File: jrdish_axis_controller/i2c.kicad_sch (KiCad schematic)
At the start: 15 parts, among them CN7 SM04B-SRSS-TB (LF)(SN), CN8 SM04B-SRSS-TB (LF)(SN), U5 LTC4311ISC6#TRPBF, U6 LM75BIMX-5/NOPB, U7 W25Q32JVSSIQ_C179173

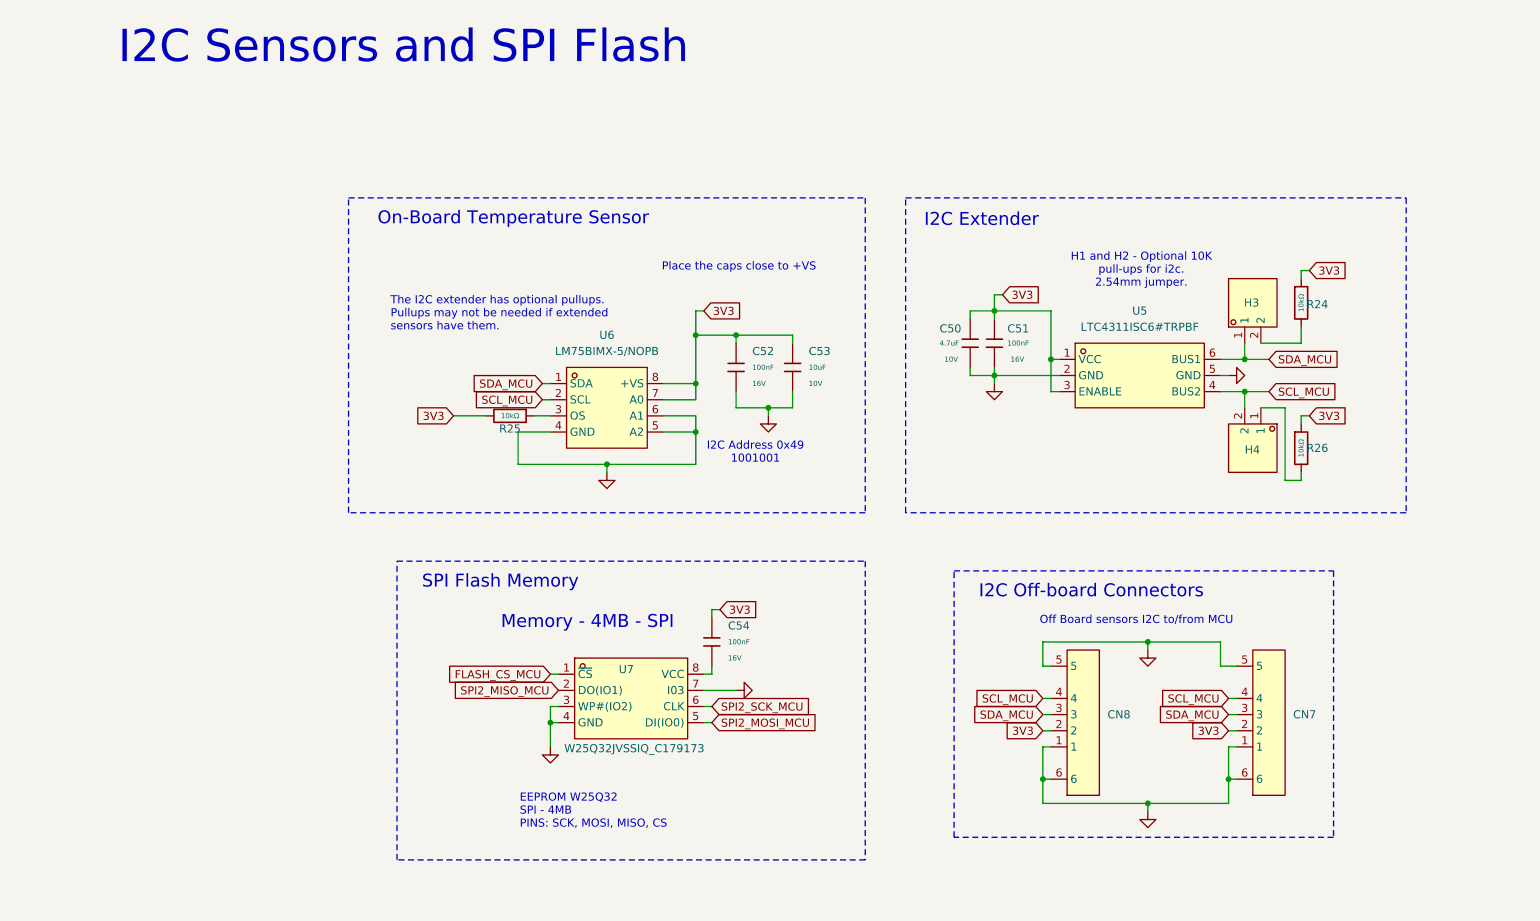
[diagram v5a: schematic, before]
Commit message: RS485 isolated areas in place
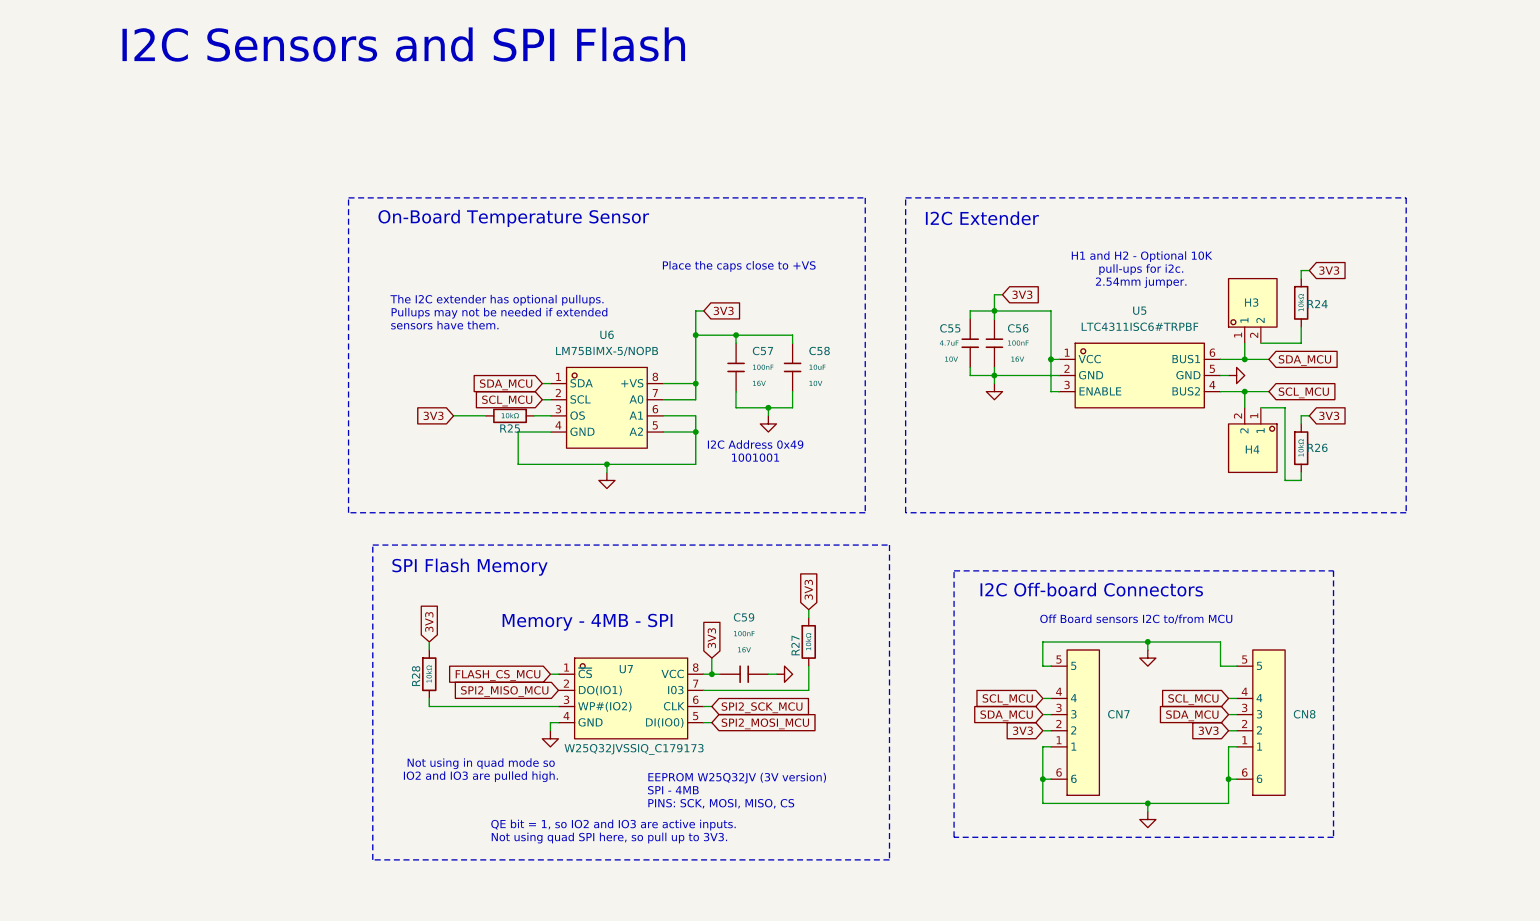
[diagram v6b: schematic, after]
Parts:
- added R27, R28: 10kΩ, PCM_JLCPCB:R_0402, symbol PCM_JLCPCB-Resistors:0402,10kΩ
- renumbered C50 to C55, C51 to C56, C52 to C57, C53 to C58, C54 to C59, CN8 to CN7, CN7 to CN8
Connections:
- net 3V3: now also U7.8 (VCC), R27.1, R28.1
- net GND: now also C59.2; no longer U7.3 (WP#(IO2)), U7.7 (I03)
- new net: R27.2, U7.7 (I03)
- new net: R28.2, U7.3 (WP#(IO2))
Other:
- note added: "EEPROM W25Q32JV (3V version) SPI - 4MB PINS: SCK, MOSI, MISO, CS"
- note added: "Not using in quad mode so IO2 and IO3 are pulled high."
- note added: "QE bit = 1, so IO2 and IO3 are active inputs. Not using quad SPI here, so pull up to 3V3."
- note removed: "EEPROM W25Q32 SPI - 4MB PINS: SCK, MOSI, MISO, CS"
- moved on the sheet: C59

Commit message: Making refinements
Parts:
- added R64: 10kΩ, PCM_JLCPCB:R_0402, symbol PCM_JLCPCB-Resistors:0402,10kΩ
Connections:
- net 3V3: now also R64.1
- net FLASH_CS_MCU: now also R64.2
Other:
- note added: "H3/H4 are the I2C pull-up resistors. Jumper should be in place by default, unless an external module supplies pull-up resistors."
- note added: "SPI Flash Memory - 4MB"
- note removed: "Memory - 4MB - SPI"
- note removed: "SPI Flash Memory"
- moved on the sheet: R28

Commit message: Making refinements
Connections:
- removed net GND: C55.2, C56.2, C57.2, C58.2, C59.2, CN7.1, CN7.5, CN7.6, CN8.1, CN8.5, CN8.6, U5.2 (GND), U5.5 (GND), U6.4 (GND), U6.5 (A2), U6.6 (A1), U7.4 (GND)
- new net: U6.4 (GND), U6.5 (A2), U6.6 (A1)
- new net: C55.2, C56.2, U5.2 (GND)
- new net: C57.2, C58.2
- new net: CN7.1, CN7.6, CN8.1, CN8.6
- new net: CN7.5, CN8.5
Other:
- note added: "NOR Flash W25Q32JV (3V version) SPI - 4MB PINS: SCK, MOSI, MISO, CS"
- note removed: "EEPROM W25Q32JV (3V version) SPI - 4MB PINS: SCK, MOSI, MISO, CS"
- title: (none) -> I2C and I2C Flash
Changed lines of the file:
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@@
 	(paper "A4")
 	(title_block
-		(date "2026-04-12")
+		(title "I2C and I2C Flash")
+		(date "2026-04-30")
 		(rev "1.0")
 		(company "JRSeti")
 	)
 	(rectangle
-		(start 66.04 100.33)
+		(start 59.69 100.33)
 		(end 147.32 149.86)
 		(stroke
@@
 		)
 	)
-	(text "EEPROM W25Q32JV (3V version) \nSPI - 4MB \nPINS: SCK, MOSI, MISO, CS"
+	(text "NOR Flash W25Q32JV (3V version) \nSPI - 4MB \nPINS: SCK, MOSI, MISO, CS"
 		(exclude_from_sim no)
 		(at 109.22 139.192 0)
@@
 			)
 		)
-		(property "Datasheet" "https://lcsc.com/product-detail/Others_JST-Sales-America__JST-Sales-America-SM04B-SRSS-TB-LF-SN_C160404.html"
+		(property "Datasheet" "https://www.lcsc.com/datasheet/C160404.pdf?spm=wm.sxq.inf.ggs&lcsc_vid=FFBaV1wHQFldUVICFgBfBVJTQVJWXgBfEQRYBAFQE1YxVlNRQFRYVVZVTllcVDtW"
 			(at 182.88 128.27 0)
 			(hide yes)
@@
 			)
 		)
-		(property "Datasheet" "https://lcsc.com/product-detail/Others_JST-Sales-America__JST-Sales-America-SM04B-SRSS-TB-LF-SN_C160404.html"
+		(property "Datasheet" "https://www.lcsc.com/datasheet/C160404.pdf?spm=wm.sxq.inf.ggs&lcsc_vid=FFBaV1wHQFldUVICFgBfBVJTQVJWXgBfEQRYBAFQE1YxVlNRQFRYVVZVTllcVDtW"
 			(at 212.09 128.27 0)
 			(hide yes)
